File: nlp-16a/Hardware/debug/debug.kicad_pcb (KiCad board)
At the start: 2 copper layers, 69.8 x 61.6 mm, 13 parts, among them J1 Conn_01x04_Female, J2 Conn_01x04_Male, J3 Conn_01x02_Male, J4 Conn_02x20_Odd_Even, J5 Conn_02x10_Odd_Even, J6 Conn_02x10_Odd_Even, J7 Conn_02x10_Odd_Even, J8 Conn_02x10_Odd_Even, U1 CH32V003F4P6

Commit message: 基板修正
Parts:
- added R2: 4.7k, Resistor_SMD:R_0603_1608Metric_Pad0.98x0.95mm_HandSolder, F.Cu at (131.4, 124.5)
- C1: footprint Capacitor_SMD:C_0201_0603Metric_Pad0.64x0.40mm_HandSolder -> Capacitor_SMD:C_0603_1608Metric_Pad1.08x0.95mm_HandSolder
- moved C1 0.83 mm to (144.1, 114.9)
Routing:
- net VDD: track 97.5 -> 103.7 mm
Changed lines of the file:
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@@
+  )
+  (footprint "Resistor_SMD:R_0603_1608Metric_Pad0.98x0.95mm_HandSolder" (layer "F.Cu")
+    (at 131.445 124.46 -90)
+    (descr "Resistor SMD 0603 (1608 Metric), square (rectangular) end terminal, IPC_7351 nominal with elongated pad for handsoldering. (Body size source: IPC-SM-782 page 72, https://www.pcb-3d.com/wordpress/wp-content/uploads/ipc-sm-782a_amendment_1_and_2.pdf), generated with kicad-footprint-generator")
+    (tags "resistor handsolder")
+    (property "Sheetfile" "ファイル: debug.kicad_sch")
+    (property "Sheetname" "")
+    (attr smd)
+    (fp_text reference "R2" (at -2.54 0) (layer "F.SilkS")
+      (effects (font (size 1 1) (thickness 0.15)))
+    )
+    (fp_text value "4.7k" (at 0 1.43 90) (layer "F.Fab")
+      (effects (font (size 1 1) (thickness 0.15)))
+    )
+    (fp_text user "${REFERENCE}" (at 0 0 90) (layer "F.Fab")
+      (effects (font (size 0.4 0.4) (thickness 0.06)))
+    )
+    (fp_line (start -0.254724 -0.5225) (end 0.254724 -0.5225) (layer "F.SilkS") (width 0.12))
+    (fp_line (start -0.254724 0.5225) (end 0.254724 0.5225) (layer "F.SilkS") (width 0.12))
+    (fp_line (start 1.65 -0.73) (end 1.65 0.73) (layer "F.CrtYd") (width 0.05))
+    (fp_line (start 1.65 0.73) (end -1.65 0.73) (layer "F.CrtYd") (width 0.05))
+    (fp_line (start -1.65 -0.73) (end 1.65 -0.73) (layer "F.CrtYd") (width 0.05))
+    (fp_line (start -1.65 0.73) (end -1.65 -0.73) (layer "F.CrtYd") (width 0.05))
+    (fp_line (start -0.8 0.4125) (end -0.8 -0.4125) (layer "F.Fab") (width 0.1))
+    (fp_line (start 0.8 -0.4125) (end 0.8 0.4125) (layer "F.Fab") (width 0.1))
+    (fp_line (start -0.8 -0.4125) (end 0.8 -0.4125) (layer "F.Fab") (width 0.1))
+    (fp_line (start 0.8 0.4125) (end -0.8 0.4125) (layer "F.Fab") (width 0.1))
+    (pad "1" smd roundrect (at -0.9125 0 270) (size 0.975 0.95) (layers "F.Cu" "F.Paste" "F.Mask") (roundrect_rratio 0.25)
+      (net 21 "Net-(J2-Pad3)") (pintype "passive"))
+    (pad "2" smd roundrect (at 0.9125 0 270) (size 0.975 0.95) (layers "F.Cu" "F.Paste" "F.Mask") (roundrect_rratio 0.25)
+      (net 1 "VDD") (pintype "passive"))
+    (model "${KICAD6_3DMODEL_DIR}/Resistor_SMD.3dshapes/R_0603_1608Metric.wrl"
+      (offset (xyz 0 0 0))
+      (scale (xyz 1 1 1))
+      (rotate (xyz 0 0 0))
+    )
   )
   (footprint "Resistor_SMD:R_0603_1608Metric_Pad0.98x0.95mm_HandSolder" (layer "F.Cu")
@@
     )
   )
-  (footprint "Capacitor_SMD:C_0201_0603Metric_Pad0.64x0.40mm_HandSolder" (layer "F.Cu")
-    (at 144.92 114.63)
-    (descr "Capacitor SMD 0201 (0603 Metric), square (rectangular) end terminal, IPC_7351 nominal with elongated pad for handsoldering. (Body size source: https://www.vishay.com/docs/20052/crcw0201e3.pdf), generated with kicad-footprint-generator")
+  (footprint "Capacitor_SMD:C_0603_1608Metric_Pad1.08x0.95mm_HandSolder" (layer "F.Cu")
+    (at 144.145 114.935)
+    (descr "Capacitor SMD 0603 (1608 Metric), square (rectangular) end terminal, IPC_7351 nominal with elongated pad for handsoldering. (Body size source: IPC-SM-782 page 76, https://www.pcb-3d.com/wordpress/wp-content/uploads/ipc-sm-782a_amendment_1_and_2.pdf), generated with kicad-footprint-generator")
     (tags "capacitor handsolder")
     (property "Sheetfile" "ファイル: debug.kicad_sch")
     (property "Sheetname" "")
     (attr smd)
-    (fp_text reference "C1" (at 0 1.575) (layer "F.SilkS")
+    (fp_text reference "C1" (at 0 -1.43) (layer "F.SilkS")
       (effects (font (size 1 1) (thickness 0.15)))
     )
-    (fp_text value "0.1u" (at 0 1.05) (layer "F.Fab")
+    (fp_text value "0.1u" (at 0 1.43) (layer "F.Fab")
       (effects (font (size 1 1) (thickness 0.15)))
     )
-    (fp_text user "${REFERENCE}" (at 0 -0.68) (layer "F.Fab")
-      (effects (font (size 0.25 0.25) (thickness 0.04)))
+    (fp_text user "${REFERENCE}" (at 0 0) (layer "F.Fab")
+      (effects (font (size 0.4 0.4) (thickness 0.06)))
     )
-    (fp_line (start -0.88 0.35) (end -0.88 -0.35) (layer "F.CrtYd") (width 0.05))
-    (fp_line (start 0.88 -0.35) (end 0.88 0.35) (layer "F.CrtYd") (width 0.05))
-    (fp_line (start -0.88 -0.35) (end 0.88 -0.35) (layer "F.CrtYd") (width 0.05))
-    (fp_line (start 0.88 0.35) (end -0.88 0.35) (layer "F.CrtYd") (width 0.05))
-    (fp_line (start 0.3 0.15) (end -0.3 0.15) (layer "F.Fab") (width 0.1))
-    (fp_line (start 0.3 -0.15) (end 0.3 0.15) (layer "F.Fab") (width 0.1))
-    (fp_line (start -0.3 0.15) (end -0.3 -0.15) (layer "F.Fab") (width 0.1))
-    (fp_line (start -0.3 -0.15) (end 0.3 -0.15) (layer "F.Fab") (width 0.1))
-    (pad "" smd roundrect (at -0.4325 0) (size 0.458 0.36) (layers "F.Paste") (roundrect_rratio 0.25))
-    (pad "" smd roundrect (at 0.4325 0) (size 0.458 0.36) (layers "F.Paste") (roundrect_rratio 0.25))
-    (pad "1" smd roundrect (at -0.4075 0) (size 0.635 0.4) (layers "F.Cu" "F.Mask") (roundrect_rratio 0.25)
+    (fp_line (start -0.146267 -0.51) (end 0.146267 -0.51) (layer "F.SilkS") (width 0.12))
+    (fp_line (start -0.146267 0.51) (end 0.146267 0.51) (layer "F.SilkS") (width 0.12))
+    (fp_line (start 1.65 -0.73) (end 1.65 0.73) (layer "F.CrtYd") (width 0.05))
+    (fp_line (start -1.65 -0.73) (end 1.65 -0.73) (layer "F.CrtYd") (width 0.05))
+    (fp_line (start 1.65 0.73) (end -1.65 0.73) (layer "F.CrtYd") (width 0.05))
+    (fp_line (start -1.65 0.73) (end -1.65 -0.73) (layer "F.CrtYd") (width 0.05))
+    (fp_line (start 0.8 0.4) (end -0.8 0.4) (layer "F.Fab") (width 0.1))
+    (fp_line (start 0.8 -0.4) (end 0.8 0.4) (layer "F.Fab") (width 0.1))
+    (fp_line (start -0.8 0.4) (end -0.8 -0.4) (layer "F.Fab") (width 0.1))
+    (fp_line (start -0.8 -0.4) (end 0.8 -0.4) (layer "F.Fab") (width 0.1))
+    (pad "1" smd roundrect (at -0.8625 0) (size 1.075 0.95) (layers "F.Cu" "F.Paste" "F.Mask") (roundrect_rratio 0.25)
       (net 1 "VDD") (pintype "passive"))
-    (pad "2" smd roundrect (at 0.4075 0) (size 0.635 0.4) (layers "F.Cu" "F.Mask") (roundrect_rratio 0.25)
+    (pad "2" smd roundrect (at 0.8625 0) (size 1.075 0.95) (layers "F.Cu" "F.Paste" "F.Mask") (roundrect_rratio 0.25)
       (net 2 "GND") (pintype "passive"))
-    (model "${KICAD6_3DMODEL_DIR}/Capacitor_SMD.3dshapes/C_0201_0603Metric.wrl"
+    (model "${KICAD6_3DMODEL_DIR}/Capacitor_SMD.3dshapes/C_0603_1608Metric.wrl"
       (offset (xyz 0 0 0))
       (scale (xyz 1 1 1))
@@
     (style (thickness 0.2) (arrow_length 1.27) (text_position_mode 0) (extension_height 0.58642) (extension_offset 0.5) keep_text_aligned)
   )
-  (segment (start 144.5125 114.63) (end 144.5125 115.3025) (width 0.25) (layer "F.Cu") (net 1))
+  (segment (start 140.97 114.935) (end 140.335 115.57) (width 0.25) (layer "F.Cu") (net 1))
+  (segment (start 144.2875 115.94) (end 143.2825 114.935) (width 0.25) (layer "F.Cu") (net 1))
   (segment (start 184.22 125.74) (end 123.13 125.74) (width 1) (layer "F.Cu") (net 1))
-  (segment (start 143.18 114.63) (end 144.5125 114.63) (width 0.25) (layer "F.Cu") (net 1))
-  (segment (start 144.5125 115.3025) (end 145.15 115.94) (width 0.25) (layer "F.Cu") (net 1))
-  (segment (start 142.875 114.935) (end 143.18 114.63) (width 0.25) (layer "F.Cu") (net 1))
+  (segment (start 143.2825 114.935) (end 140.97 114.935) (width 0.25) (layer "F.Cu") (net 1))
+  (segment (start 146.96 115.94) (end 144.2875 115.94) (width 0.25) (layer "F.Cu") (net 1))
   (segment (start 123.13 125.74) (end 123.12 125.73) (width 1) (layer "F.Cu") (net 1))
-  (segment (start 142.875 115.57) (end 142.875 114.935) (width 0.25) (layer "F.Cu") (net 1))
-  (segment (start 145.15 115.94) (end 146.96 115.94) (width 0.25) (layer "F.Cu") (net 1))
-  (via (at 142.875 115.57) (size 0.8) (drill 0.4) (layers "F.Cu" "B.Cu") (net 1))
+  (via (at 140.335 115.57) (size 0.8) (drill 0.4) (layers "F.Cu" "B.Cu") (net 1))
+  (segment (start 121.92 119.38) (end 123.19 119.38) (width 0.25) (layer "B.Cu") (net 1))
+  (segment (start 123.83 119.375) (end 123.83 114.3) (width 0.25) (layer "B.Cu") (net 1))
   (segment (start 123.12 125.72) (end 121.91 125.72) (width 0.25) (layer "B.Cu") (net 1))
-  (segment (start 121.92 119.38) (end 139.065 119.38) (width 0.25) (layer "B.Cu") (net 1))
+  (segment (start 123.19 119.38) (end 123.825 119.38) (width 0.25) (layer "B.Cu") (net 1))
+  (segment (start 140.335 115.57) (end 140.335 118.11) (width 0.25) (layer "B.Cu") (net 1))
   (segment (start 121.285 125.095) (end 121.285 120.015) (width 0.25) (layer "B.Cu") (net 1))
-  (segment (start 139.065 119.38) (end 142.875 115.57) (width 0.25) (layer "B.Cu") (net 1))
+  (segment (start 123.825 119.38) (end 123.83 119.375) (width 0.25) (layer "B.Cu") (net 1))
   (segment (start 121.91 125.72) (end 121.285 125.095) (width 0.25) (layer "B.Cu") (net 1))
+  (segment (start 140.335 118.11) (end 139.065 119.38) (width 0.25) (layer "B.Cu") (net 1))
+  (segment (start 139.065 119.38) (end 123.19 119.38) (width 0.25) (layer "B.Cu") (net 1))
   (segment (start 121.285 120.015) (end 121.92 119.38) (width 0.25) (layer "B.Cu") (net 1))
+  (segment (start 146.251875 114.64) (end 146.96 114.64) (width 0.25) (layer "F.Cu") (net 2))
+  (segment (start 145.0075 114.935) (end 145.956875 114.935) (width 0.25) (layer "F.Cu") (net 2))
   (segment (start 123.12 128.27) (end 184.21 128.27) (width 1) (layer "F.Cu") (net 2))
+  (segment (start 145.956875 114.935) (end 146.251875 114.64) (width 0.25) (layer "F.Cu") (net 2))
   (segment (start 184.21 128.27) (end 184.22 128.28) (width 1) (layer "F.Cu") (net 2))
   (segment (start 148.25 114.64) (end 148.59 114.3) (width 0.25) (layer "F.Cu") (net 2))
-  (segment (start 145.3375 114.64) (end 145.3275 114.63) (width 0.25) (layer "F.Cu") (net 2))
   (segment (start 146.96 114.64) (end 148.25 114.64) (width 0.25) (layer "F.Cu") (net 2))
-  (segment (start 146.96 114.64) (end 145.3375 114.64) (width 0.25) (layer "F.Cu") (net 2))
   (via (at 148.59 114.3) (size 0.8) (drill 0.4) (layers "F.Cu" "B.Cu") (free) (net 2))
   (via (at 148.59 113.03) (size 0.8) (drill 0.4) (layers "F.Cu" "B.Cu") (free) (net 2))

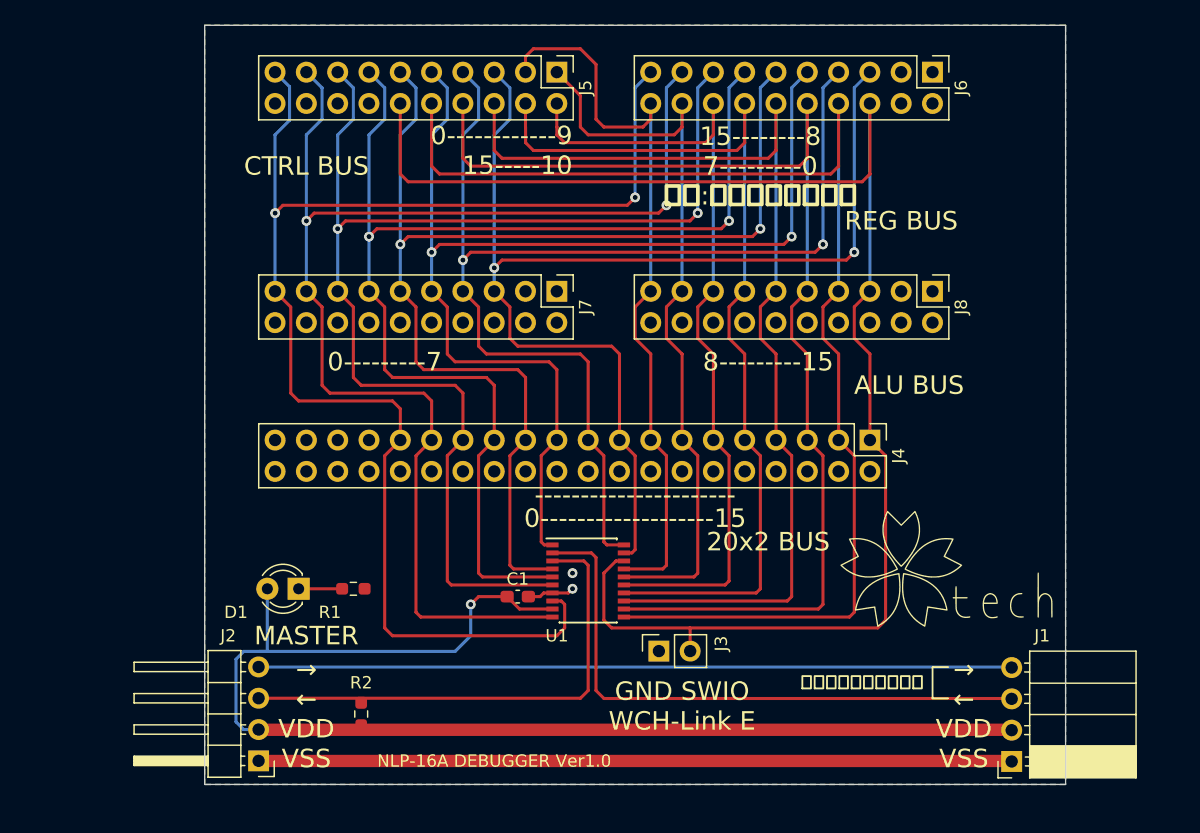
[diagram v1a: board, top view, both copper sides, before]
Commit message: デバッガ基板の設計完了
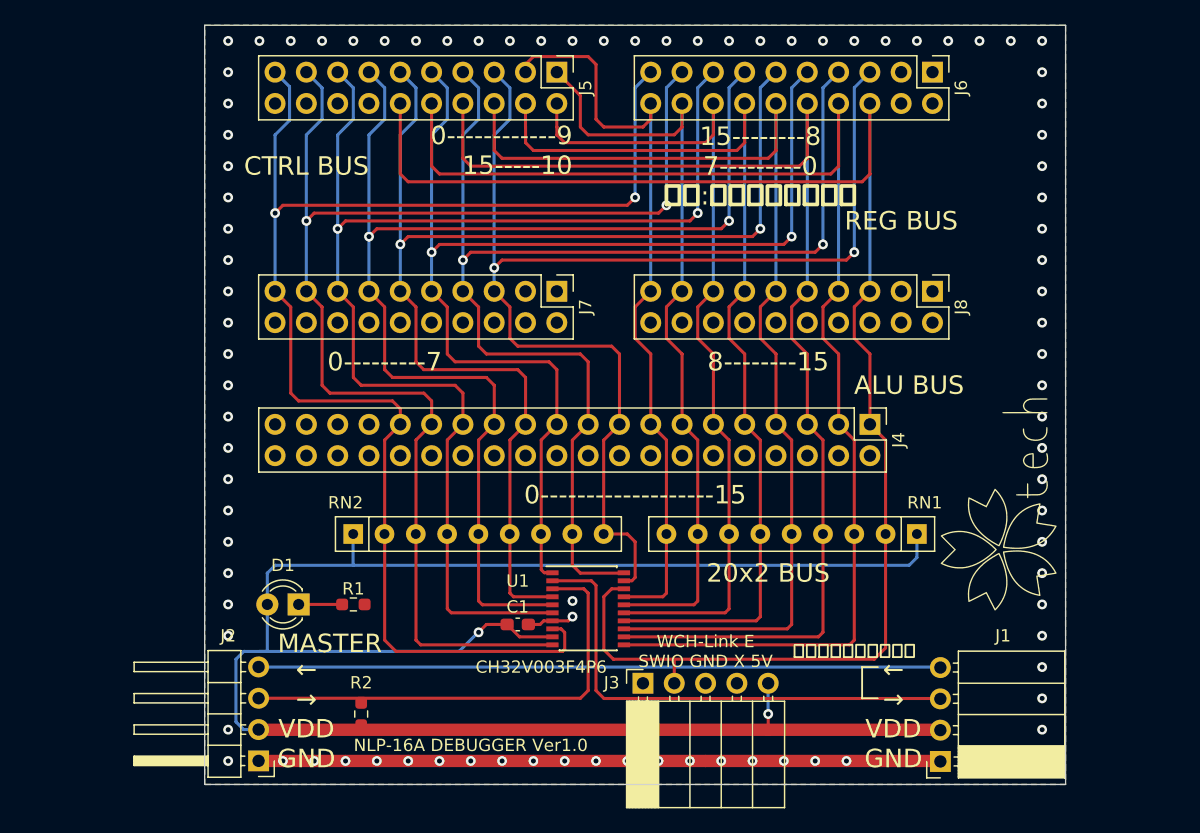
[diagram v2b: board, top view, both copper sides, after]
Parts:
- added RN1: R_Network08_US, Resistor_THT:R_Array_SIP9, F.Cu at (176.5, 109.9)
- added RN2: R_Network08_US, Resistor_THT:R_Array_SIP9, F.Cu at (130.8, 109.9)
- J3: value Conn_01x02_Male -> Conn_01x05_Female; footprint Connector_PinSocket_2.54mm:PinSocket_1x02_P2.54mm_Vertical -> Connector_PinSocket_2.54mm:PinSocket_1x05_P2.54mm_Horizontal
- moved G*** 7.41 mm to (183.5, 106.7), turned to 90 degrees
- moved J1 5.78 mm to (178.4, 128.3)
- moved J3 2.91 mm to (154.3, 122.0)
- moved C1 2.26 mm to (144.1, 117.2)
- moved U1 2.26 mm to (149.9, 115.9)
- moved J4 1.28 mm to (172.7, 101.0)
- moved D1 1.27 mm to (126.4, 115.6)
- moved R1 1.27 mm to (130.8, 115.6)
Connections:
- J3 pad 1: GND -> unconnected-(J3-Pad1)
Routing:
- net VDD: track 103.7 -> 158.2 mm, vias 1 -> 2
- net Net-(J1-Pad3): track 48.5 -> 40.4 mm
- net GND: track 64.9 -> 59.2 mm, vias 2 -> 92
- net Net-(J1-Pad4): track 61.1 -> 55.3 mm
- net DATA6: track 94.3 -> 99.0 mm
- net DATA7: track 94.9 -> 99.3 mm
- net DATA15: track 124.7 -> 127.5 mm
- net DATA4: track 96.8 -> 99.1 mm
- net DATA5: track 93.0 -> 95.2 mm
- net DATA2: track 101.9 -> 104.2 mm
- net DATA14: track 105.4 -> 107.7 mm
- net DATA13: track 95.9 -> 98.2 mm
- net DATA10: track 67.3 -> 69.6 mm
- net DATA1: track 106.4 -> 108.6 mm
- net Net-(J2-Pad3): track 40.2 -> 37.9 mm
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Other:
- board text added: "8--------15"
- board text added: "CH32V003F4P6"
- board text added: "WCH-Link E SWIO GND X 5V"
- board text added: "← → VDD GND"
- board text removed: "----------------------"
- board text removed: "8---------15"
- board text removed: "GND SWIO WCH-Link E"
- board text removed: "→ ← VDD VSS"

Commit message: デバッガ基板の設計今度こそ完了
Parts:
- J1: value Conn_01x04_Female -> Conn_01x06_Male; footprint Connector_PinSocket_2.54mm:PinSocket_1x04_P2.54mm_Horizontal -> Connector_PinHeader_2.54mm:PinHeader_1x06_P2.54mm_Horizontal
- J2: value Conn_01x04_Male -> Conn_01x06_Female; footprint Connector_PinHeader_2.54mm:PinHeader_1x04_P2.54mm_Horizontal -> Connector_PinSocket_2.54mm:PinSocket_1x06_P2.54mm_Horizontal
- J3: value Conn_01x05_Female -> Conn_01x06_Female; footprint Connector_PinSocket_2.54mm:PinSocket_1x05_P2.54mm_Horizontal -> Connector_PinSocket_2.54mm:PinSocket_1x06_P2.54mm_Horizontal
- moved J2 55.4 mm to (178.5, 128.2)
- moved J1 55.3 mm to (123.1, 128.3)
- moved G*** 2.62 mm to (184.2, 104.1)
- moved D1 2.53 mm to (128.9, 115.6)
- moved R1 1.56 mm to (132.1, 116.5), turned to -90 degrees
- moved J3 1.25 mm to (153.1, 122.0)
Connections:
- J3 pad 2: DATA15 -> unconnected-(J3-Pad2)
- J3 pad 3: GND -> DATA15
- J3 pad 4: unconnected-(J3-Pad4) -> GND
- J3 pad 5: VDD -> unconnected-(J3-Pad5)
- R2 pad 1: Net-(J2-Pad3) -> Net-(J1-Pad3)
- U1 pad 2: Net-(J1-Pad3) -> Net-(J2-Pad3)
- U1 pad 3: Net-(J2-Pad3) -> Net-(J1-Pad3)
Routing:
- net Net-(J2-Pad3): track 37.9 -> 40.4 mm
- net Net-(J1-Pad3): track 40.4 -> 37.9 mm
